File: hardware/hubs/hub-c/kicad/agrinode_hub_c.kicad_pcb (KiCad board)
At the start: 2 copper layers, 130 x 96 mm, 119 parts, among them J1 DC 12V 5.5/2.1, J10 LTE MODULE, J2 DC IN 7-24V, J3 SOLAR 6-24V, J4 USB 5V / PROG, J5 BAT NTC 10k, J6 PROG, J7 I2C, J8 LED STRIP WS2813, J9 RS-485, Q1 AO3401A, Q2 AO3401A, Q3 MMBT3904, Q4 MMBT3904, Q5 BSS138, Q6 MMBT3904, Q7 AO3401A, Q8 MMBT3904, Q9 MMBT3904, SW1 RESET, SW2 BOOT / PAIR, U1 LM2596S-5.0, U2 TP4056, U3 MIC29302WU, U4 ESP32-WROOM-32E-N8, U5 CH340C, U6 DS3231MZ, U7 MAX3485ESA, U8 MIC29302WU

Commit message: hubs: routing progress snapshot
Co-Authored-By: Claude Opus 5.5 <noreply@anthropic.com>
Claude-Session: https://claude.ai/code/session_014J7amXZ5Y6AZWEh5CjDNja
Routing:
- net GND: track 0.00 -> 839.1 mm, vias 0 -> 6
- net +3V3: track 0.00 -> 316.6 mm, vias 0 -> 6
- net V5: track 0.00 -> 220.8 mm, vias 0 -> 3
- net VSYS: track 0.00 -> 210.3 mm, vias 0 -> 3
- net MODEM_TXD: track 0.00 -> 203.7 mm, vias 0 -> 8
- net /Power - 12V, solar and USB inputs, 18650 charger, rails/VUSB_RAW: track 0.00 -> 140.4 mm, vias 0 -> 5
- net MODEM_EN: track 0.00 -> 131.6 mm, vias 0 -> 5
- net /ESP32, programming, buttons, RTC, LED strip, buzzer/BUZ_B: track 0.00 -> 126.5 mm, vias 0 -> 3
- net MODEM_PWRKEY_CTL: track 0.00 -> 126.4 mm, vias 0 -> 8
- net /ESP32, programming, buttons, RTC, LED strip, buzzer/ESP_EN: track 0.00 -> 107.9 mm, vias 0 -> 1
- net /RS-485 and uplink/RS485_A: track 0.00 -> 106.2 mm, vias 0 -> 3
- net /Power - 12V, solar and USB inputs, 18650 charger, rails/VBAT: track 0.00 -> 104.3 mm, vias 0 -> 4
- net /Power - 12V, solar and USB inputs, 18650 charger, rails/BATT_CELL: track 0.00 -> 102.5 mm, vias 0 -> 2
- net /ESP32, programming, buttons, RTC, LED strip, buzzer/I2C_SCL: track 0.00 -> 100.6 mm, vias 0 -> 2
- net /ESP32, programming, buttons, RTC, LED strip, buzzer/I2C_SDA: track 0.00 -> 95.8 mm, vias 0 -> 3
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- added copper zone on B.Cu, net GND
- added copper zone on F.Cu, net GND

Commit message: hubs: routing progress snapshot
Co-Authored-By: Claude Opus 5.5 <noreply@anthropic.com>
Claude-Session: https://claude.ai/code/session_014J7amXZ5Y6AZWEh5CjDNja
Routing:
- net GND: track 839.1 -> 0.00 mm, vias 6 -> 0
- net +3V3: track 316.6 -> 0.00 mm, vias 6 -> 0
- net V5: track 220.8 -> 0.00 mm, vias 3 -> 0
- net VSYS: track 210.3 -> 0.00 mm, vias 3 -> 0
- net MODEM_TXD: track 203.7 -> 0.00 mm, vias 8 -> 0
- net /Power - 12V, solar and USB inputs, 18650 charger, rails/VUSB_RAW: track 140.4 -> 0.00 mm, vias 5 -> 0
- net MODEM_EN: track 131.6 -> 0.00 mm, vias 5 -> 0
- net /ESP32, programming, buttons, RTC, LED strip, buzzer/BUZ_B: track 126.5 -> 0.00 mm, vias 3 -> 0
- net MODEM_PWRKEY_CTL: track 126.4 -> 0.00 mm, vias 8 -> 0
- net /ESP32, programming, buttons, RTC, LED strip, buzzer/ESP_EN: track 107.9 -> 0.00 mm, vias 1 -> 0
- net /RS-485 and uplink/RS485_A: track 106.2 -> 0.00 mm, vias 3 -> 0
- net /Power - 12V, solar and USB inputs, 18650 charger, rails/VBAT: track 104.3 -> 0.00 mm, vias 4 -> 0
- net /Power - 12V, solar and USB inputs, 18650 charger, rails/BATT_CELL: track 102.5 -> 0.00 mm, vias 2 -> 0
- net /ESP32, programming, buttons, RTC, LED strip, buzzer/I2C_SCL: track 100.6 -> 0.00 mm, vias 2 -> 0
- net /ESP32, programming, buttons, RTC, LED strip, buzzer/I2C_SDA: track 95.8 -> 0.00 mm, vias 3 -> 0
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- removed copper zone on B.Cu, net GND
- removed copper zone on F.Cu, net GND

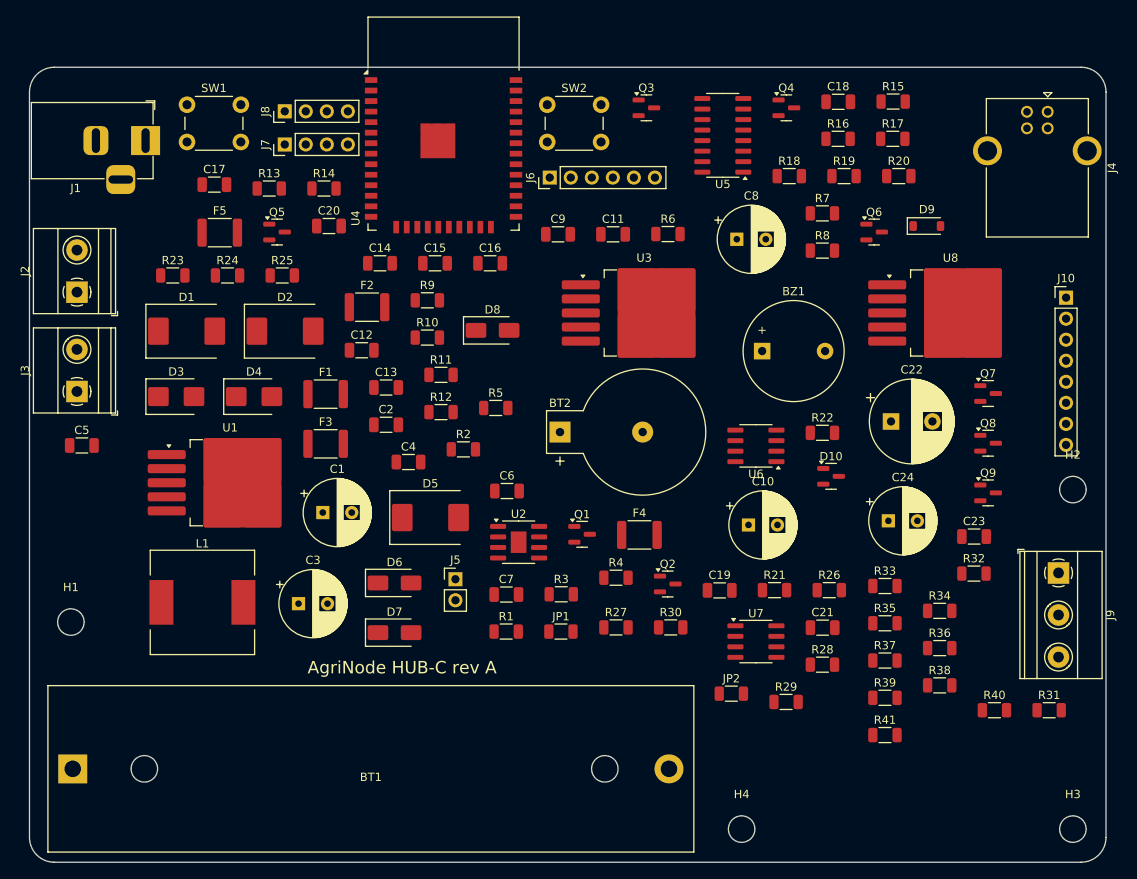
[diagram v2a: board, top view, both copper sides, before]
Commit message: finish_router: local rip-up (remove only blocking segments); routing snapshot
Co-Authored-By: Claude Opus 5.5 <noreply@anthropic.com>
Claude-Session: https://claude.ai/code/session_014J7amXZ5Y6AZWEh5CjDNja
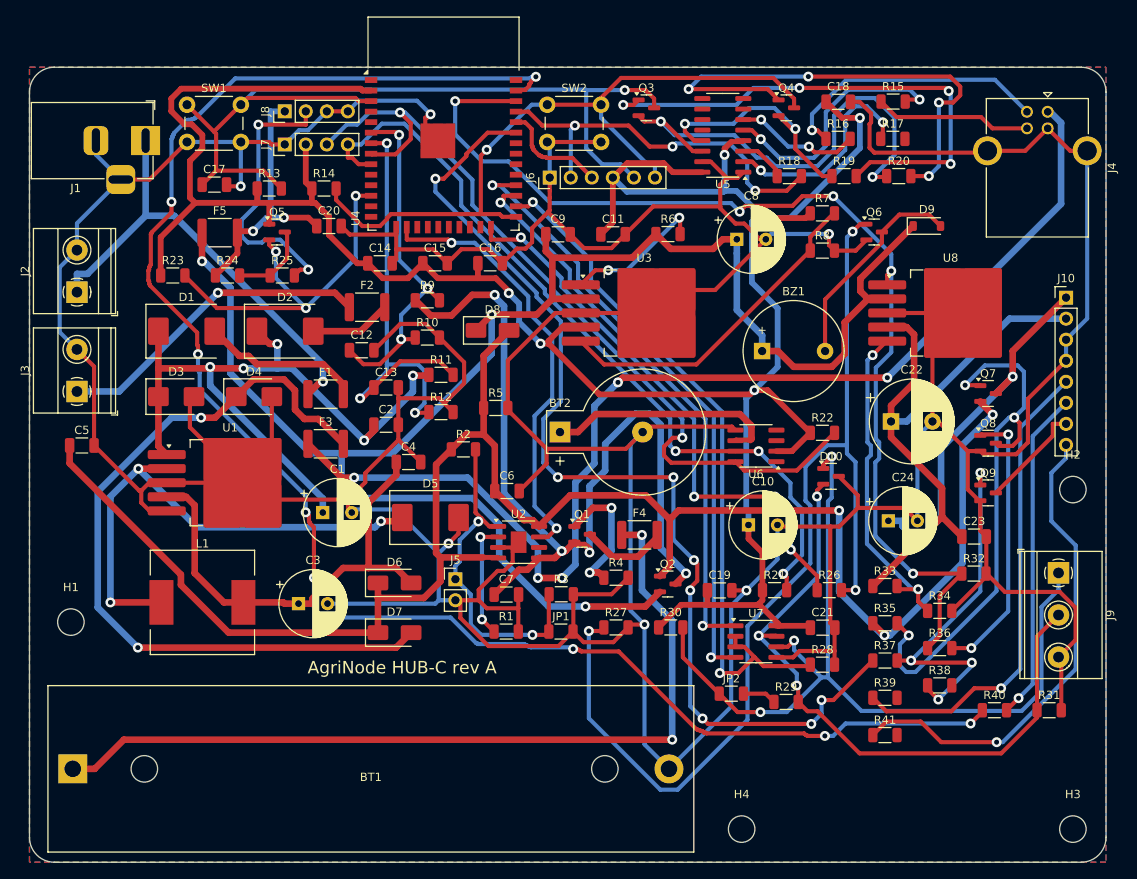
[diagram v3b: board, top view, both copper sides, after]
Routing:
- net GND: track 0.00 -> 839.1 mm, vias 0 -> 6
- net +3V3: track 0.00 -> 316.6 mm, vias 0 -> 6
- net V5: track 0.00 -> 220.8 mm, vias 0 -> 3
- net VSYS: track 0.00 -> 210.3 mm, vias 0 -> 3
- net MODEM_TXD: track 0.00 -> 203.7 mm, vias 0 -> 8
- net /Power - 12V, solar and USB inputs, 18650 charger, rails/VUSB_RAW: track 0.00 -> 140.4 mm, vias 0 -> 5
- net MODEM_EN: track 0.00 -> 131.6 mm, vias 0 -> 5
- net /ESP32, programming, buttons, RTC, LED strip, buzzer/BUZ_B: track 0.00 -> 126.5 mm, vias 0 -> 3
- net MODEM_PWRKEY_CTL: track 0.00 -> 126.4 mm, vias 0 -> 8
- net /ESP32, programming, buttons, RTC, LED strip, buzzer/ESP_EN: track 0.00 -> 107.9 mm, vias 0 -> 1
- net /RS-485 and uplink/RS485_A: track 0.00 -> 106.2 mm, vias 0 -> 3
- net /Power - 12V, solar and USB inputs, 18650 charger, rails/VBAT: track 0.00 -> 104.3 mm, vias 0 -> 4
- net /Power - 12V, solar and USB inputs, 18650 charger, rails/BATT_CELL: track 0.00 -> 102.5 mm, vias 0 -> 2
- net /ESP32, programming, buttons, RTC, LED strip, buzzer/I2C_SCL: track 0.00 -> 100.6 mm, vias 0 -> 2
- net /ESP32, programming, buttons, RTC, LED strip, buzzer/I2C_SDA: track 0.00 -> 95.8 mm, vias 0 -> 3
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- added copper zone on B.Cu, net GND
- added copper zone on F.Cu, net GND

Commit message: hubs: open a 6 mm routing channel beside the ESP32 right column (BOOT button and PROG header moved); pin the LDO bulk cap
Co-Authored-By: Claude Opus 5.5 <noreply@anthropic.com>
Claude-Session: https://claude.ai/code/session_014J7amXZ5Y6AZWEh5CjDNja
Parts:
- moved R30 46.8 mm to (173.1, 127.6)
- moved C8 44.0 mm to (135.3, 114.8)
- moved D7 42.6 mm to (57.6, 96.3)
- moved C10 41.1 mm to (106.2, 77.8)
- moved D8 40.9 mm to (127.1, 116.8)
- moved R31 38.6 mm to (134.8, 131.6)
- moved D9 37.1 mm to (143.5, 103.2)
- moved R7 26.5 mm to (145.8, 94.1)
- moved R8 26.5 mm to (145.8, 98.6)
- moved R27 25.4 mm to (145.6, 112.1)
- moved R22 25.0 mm to (127.9, 111.6)
- moved R2 24.5 mm to (113.3, 118.1)
- moved R3 23.8 mm to (106.3, 91.1)
- moved C9 21.4 mm to (135.2, 70.2)
- moved C7 18.2 mm to (102.4, 96.2)
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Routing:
- net GND: track 839.1 -> 0.00 mm, vias 6 -> 0
- net +3V3: track 316.6 -> 0.00 mm, vias 6 -> 0
- net V5: track 220.8 -> 0.00 mm, vias 3 -> 0
- net VSYS: track 210.3 -> 0.00 mm, vias 3 -> 0
- net MODEM_TXD: track 203.7 -> 0.00 mm, vias 8 -> 0
- net /Power - 12V, solar and USB inputs, 18650 charger, rails/VUSB_RAW: track 140.4 -> 0.00 mm, vias 5 -> 0
- net MODEM_EN: track 131.6 -> 0.00 mm, vias 5 -> 0
- net /ESP32, programming, buttons, RTC, LED strip, buzzer/BUZ_B: track 126.5 -> 0.00 mm, vias 3 -> 0
- net MODEM_PWRKEY_CTL: track 126.4 -> 0.00 mm, vias 8 -> 0
- net /ESP32, programming, buttons, RTC, LED strip, buzzer/ESP_EN: track 107.9 -> 0.00 mm, vias 1 -> 0
- net /RS-485 and uplink/RS485_A: track 106.2 -> 0.00 mm, vias 3 -> 0
- net /Power - 12V, solar and USB inputs, 18650 charger, rails/VBAT: track 104.3 -> 0.00 mm, vias 4 -> 0
- net /Power - 12V, solar and USB inputs, 18650 charger, rails/BATT_CELL: track 102.5 -> 0.00 mm, vias 2 -> 0
- net /ESP32, programming, buttons, RTC, LED strip, buzzer/I2C_SCL: track 100.6 -> 0.00 mm, vias 2 -> 0
- net /ESP32, programming, buttons, RTC, LED strip, buzzer/I2C_SDA: track 95.8 -> 0.00 mm, vias 3 -> 0
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- removed copper zone on B.Cu, net GND
- removed copper zone on F.Cu, net GND
